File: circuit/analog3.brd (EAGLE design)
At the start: 56.2 x 50.8 mm, 76 parts, among them IC1 OP07C, IC2 74HC4052D, IC3 AD8603UJ, IC4 AD8221R, IC5 AD8221R, IC6 LM258, IC7 LM258

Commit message: - начали делать цифровую часть
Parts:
- added C27: 100n, rcl:C0603
- moved X4 0.63 mm to (22.9, 4.45), turned to 0 degrees
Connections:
- net +2.5V0: now also C27.1
- net GNDA: now also C27.2
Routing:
- net RA: track 4.55 -> 8.62 mm
- net GNDA: track 366.9 -> 369.2 mm
- net +2.5V0: track 55.0 -> 57.2 mm
- net RB: track 5.07 -> 3.54 mm
- added copper zone on layer 16, net GNDA

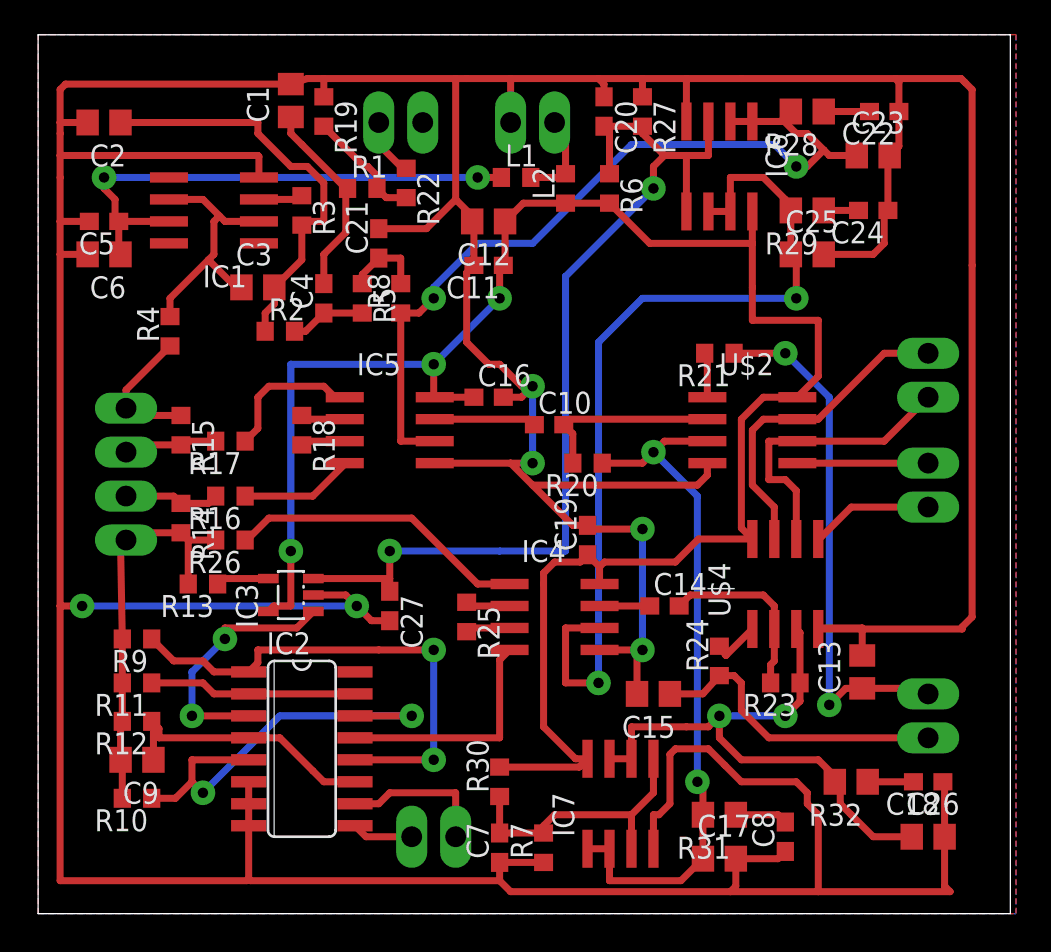
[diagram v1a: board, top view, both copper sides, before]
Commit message: - переделали аналоговую часть под более быстрый усилитель -  убрали неработающие микроиндуктивности, поставили индуктивность побольше - подставили дополнительный конденсатор на +2.5V
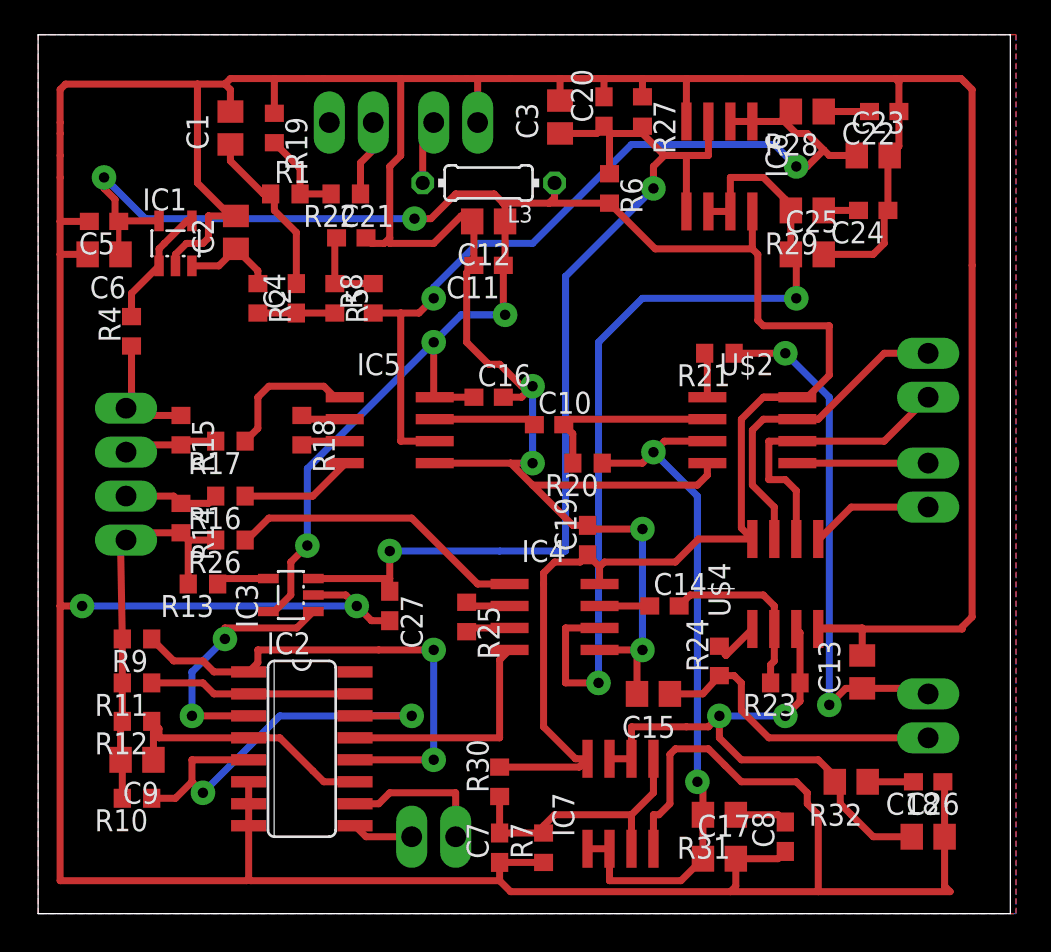
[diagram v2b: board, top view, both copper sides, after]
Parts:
- removed L1, L2: MMZ1608B102C, rcl:R0603
- removed R3: 22k, rcl:R0603
- added L3: (no value), rcl:0204/7
- C2: value 47p -> 100p
- C3: value 100p -> 10mk
- IC1: value OP07C -> AD8603UJ; device analog-devices:SO8 -> analog-devices:SOT23-5
- R18, R25: value 27k -> 18k
- moved C3 20.0 mm to (30.2, 46.0), turned to 90 degrees
- moved C2 9.92 mm to (11.4, 39.4), turned to 90 degrees
- moved R1 4.46 mm to (14.3, 41.6)
- moved X2 4.45 mm to (24.1, 45.7), turned to 180 degrees
- moved C1 3.84 mm to (11.1, 45.4)
- moved R22 3.55 mm to (17.8, 41.6), turned to 180 degrees
- moved R19 3.01 mm to (13.7, 45.4)
- moved IC1 2.93 mm to (7.94, 38.7), turned to 0 degrees
- moved X8 2.86 mm to (18.1, 45.7), turned to 0 degrees
- moved R2 2.29 mm to (12.7, 35.6), turned to 270 degrees
- moved R4 2.22 mm to (5.40, 33.7)
- moved C21 1.62 mm to (18.1, 39.1), turned to 0 degrees
- moved C4 1.59 mm to (14.9, 35.6)
- moved R5 1.59 mm to (17.1, 35.6)
- moved R8 1.59 mm to (19.4, 35.6)
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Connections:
- removed net N$7: C5.1, C6.1, IC1.7, L1.1
- removed net V+: C11.1, C12.1, C16.1, C19.1, IC3.5, IC4.8, IC5.8, IC6.8, IC7.8, L2.1, R30.2, R6.2, U$2.8, U$4.8
- net +2.5V0: now also C20.1, C3.1; no longer C20.2
- net +5V: now also C11.1, C12.1, C16.1, C19.1, C5.1, C6.1, IC1.5, IC3.5, IC4.8, IC5.8, IC6.8, IC7.8, L3.1, R30.2, R6.2, U$2.8, U$4.8; no longer L1.2, L2.2, X2.1
- net GNDA: now also C20.2, C3.2, IC1.2; no longer C20.1, IC1.4
- net N$3: now also IC1.3; no longer C3.2, R3.2
- net N$5: now also IC1.1, IC1.4; no longer C3.1, IC1.2, IC1.6
- net N$6: now also L3.2, X2.1; no longer IC1.3, R3.1
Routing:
- net +5V: track 5.32 -> 146.3 mm, vias 0 -> 5
- net V+: track 111.4 -> 0.00 mm, vias 3 -> 0
- net N$7: track 30.7 -> 0.00 mm, vias 2 -> 0
- net N$3: track 24.2 -> 5.49 mm
- net N$5: track 15.3 -> 7.14 mm
- net GNDA: track 369.2 -> 376.6 mm
- net +2.5V0: track 57.2 -> 59.6 mm
- net N$2: track 11.6 -> 9.87 mm
- net +2.5V1: track 48.0 -> 49.6 mm
- net N$34: track 6.90 -> 5.37 mm
- net N$6: track 2.57 -> 3.76 mm
- net N$19: track 8.00 -> 7.08 mm
- net GENERATOR: track 3.57 -> 4.43 mm

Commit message: - перед тем, как будем заводить SPI
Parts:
- removed C7: 100n, rcl:C0603
- removed R1: 12k, rcl:R0603
- C1: value 100p -> 10mk
- C10, C14, C4: value 100n -> 1mk
- C13, C15: value 100p -> 150p
- R27, R6: value 100k -> 120k
- moved C1 44.2 mm to (27.0, 4.13), turned to 270 degrees
- moved C6 7.96 mm to (7.62, 45.1), turned to 90 degrees
- moved C5 5.32 mm to (5.40, 45.1), turned to 90 degrees
- moved R30 0.45 mm to (27.0, 7.94)
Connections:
- removed net N$2: C1.1, C4.2, R1.1
- net GNDA: no longer C7.1
- net N$34: now also C4.2; no longer R1.2
- net N$41: now also C1.1; no longer C7.2
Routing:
- net N$34: track 5.37 -> 10.7 mm
- net N$2: track 9.87 -> 14.6 mm
- net +5V: track 146.3 -> 144.2 mm
- net GNDA: track 376.6 -> 375.1 mm

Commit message: - версия, которая почти успевает считать sin, cos свертку
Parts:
- C9: value 4.7p -> 0p
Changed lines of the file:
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@@
 <element name="R12" library="rcl" package="R0603" value="100k" x="5.715" y="11.1125" rot="R180"/>
 <element name="R13" library="rcl" package="R0603" value="1k" x="9.525" y="19.05" rot="R180"/>
-<element name="C9" library="rcl" package="C0805" value="4.7p" x="5.715" y="8.89" rot="R180"/>
+<element name="C9" library="rcl" package="C0805" value="0p" x="5.715" y="8.89" rot="R180"/>
 <element name="X1" library="con-phoenix-254" package="4POL254" value="" x="5.08" y="25.4" rot="MR270">
 <attribute name="OC_NEWARK" value="unknown" x="45.72" y="-13.97" size="1.778" layer="28" rot="MR270" display="off"/>

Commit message: C2 100 p -> 33 p R30 100 K -> 56 K - перенастроили соответственно уровни усиления
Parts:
- C2: value 100p -> 33p
- R30: value 100k -> 56k
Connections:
- net +1.6V1 renamed +2.2V1
- net +1.6V2 renamed +2.2V2
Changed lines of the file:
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@@
 <elements>
 <element name="R2" library="rcl" package="R0603" value="12k" x="12.7" y="35.56" rot="R270"/>
-<element name="C2" library="rcl" package="C0805" value="100p" x="11.43" y="39.37" rot="R90"/>
+<element name="C2" library="rcl" package="C0805" value="33p" x="11.43" y="39.37" rot="R90"/>
 <element name="C4" library="rcl" package="C0603" value="1mk" x="14.9225" y="35.56" rot="R90"/>
 <element name="C5" library="rcl" package="C0603" value="100n" x="5.3975" y="45.085" rot="R90"/>
@@
 <element name="IC7" library="linear" package="SO08" value="LM258" x="33.655" y="6.35"/>
 <element name="R7" library="rcl" package="R0603" value="47k" x="29.21" y="3.81" rot="R90"/>
-<element name="R30" library="rcl" package="R0603" value="100k" x="26.9875" y="7.9375" rot="R90"/>
+<element name="R30" library="rcl" package="R0603" value="56k" x="26.9875" y="7.9375" rot="R90"/>
 <element name="R31" library="rcl" package="R0805" value="5" x="39.37" y="5.715" rot="R180"/>
 <element name="C8" library="rcl" package="C0603" value="1mk" x="43.18" y="4.445" rot="R90"/>
@@
 <wire x1="50.585" y1="7.62" x2="47.94" y2="7.62" width="0.4064" layer="1"/>
 </signal>
-<signal name="+1.6V1">
+<signal name="+2.2V1">
 <contactref element="IC7" pad="1"/>
 <contactref element="R31" pad="2"/>
@@
 <wire x1="38.42" y1="3.175" x2="38.42" y2="5.715" width="0.4064" layer="1"/>
 </signal>
-<signal name="+1.6V2">
+<signal name="+2.2V2">
 <contactref element="IC7" pad="6"/>
 <contactref element="IC7" pad="7"/>

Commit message: - перед коррекцией по трем параметрам
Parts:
- C18, C8: value 1mk -> 4.7mk
- R31, R32: value 5 -> 22
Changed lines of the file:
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@@
 <element name="R7" library="rcl" package="R0603" value="47k" x="29.21" y="3.81" rot="R90"/>
 <element name="R30" library="rcl" package="R0603" value="56k" x="26.9875" y="7.9375" rot="R90"/>
-<element name="R31" library="rcl" package="R0805" value="5" x="39.37" y="5.715" rot="R180"/>
-<element name="C8" library="rcl" package="C0603" value="1mk" x="43.18" y="4.445" rot="R90"/>
+<element name="R31" library="rcl" package="R0805" value="22" x="39.37" y="5.715" rot="R180"/>
+<element name="C8" library="rcl" package="C0603" value="4.7mk" x="43.18" y="4.445" rot="R90"/>
 <element name="C17" library="rcl" package="C0805" value="47n" x="39.37" y="3.175"/>
-<element name="R32" library="rcl" package="R0805" value="5" x="46.99" y="7.62" rot="R180"/>
-<element name="C18" library="rcl" package="C0603" value="1mk" x="51.435" y="7.62" rot="R180"/>
+<element name="R32" library="rcl" package="R0805" value="22" x="46.99" y="7.62" rot="R180"/>
+<element name="C18" library="rcl" package="C0603" value="4.7mk" x="51.435" y="7.62" rot="R180"/>
 <element name="C26" library="rcl" package="C0805" value="47n" x="51.435" y="4.445"/>
 <element name="C27" library="rcl" package="C0603" value="100n" x="20.32" y="17.78" rot="R270"/>

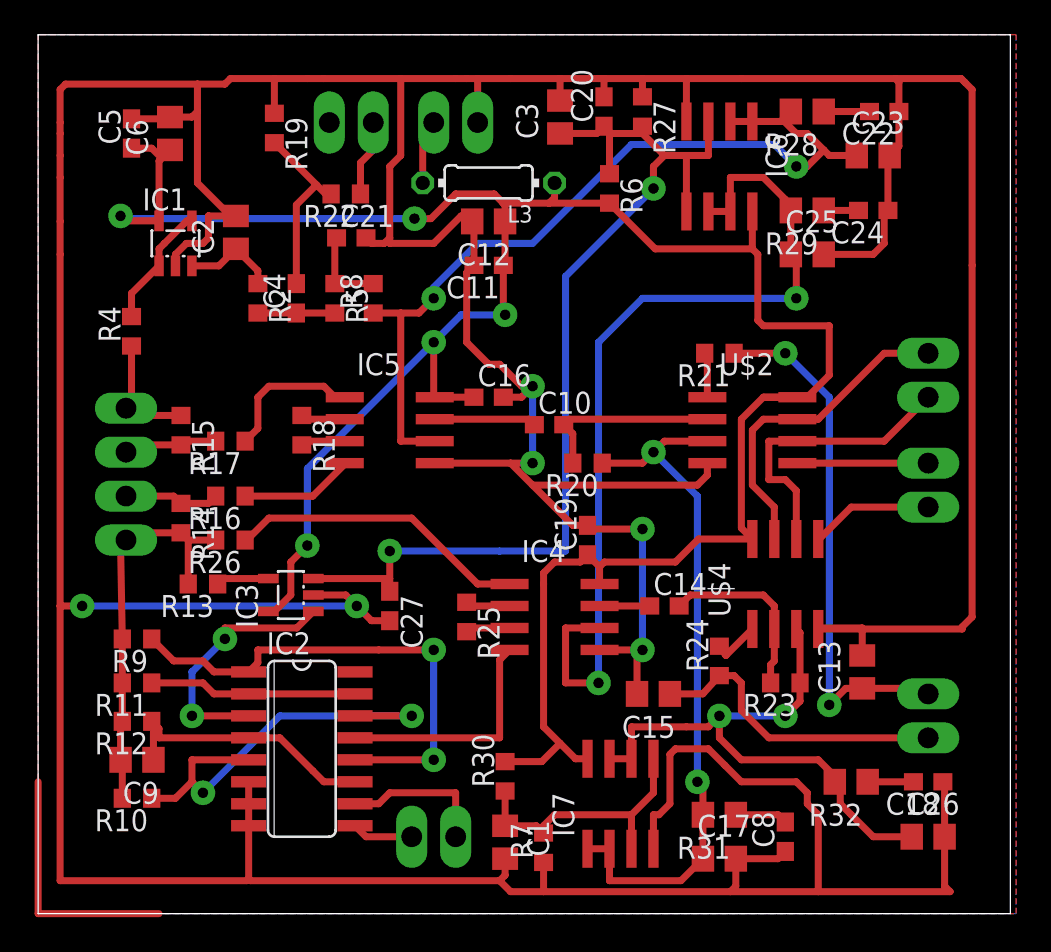
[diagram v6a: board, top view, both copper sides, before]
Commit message: - на цифровой схеме добавили разъем для Nokia 5110, коннекторы для переключения питания, объединили восточный разъем - на аналоговой схеме добавили включение 3.3 nF конденсатор, для фильтрации высокочастотных шумов ADC
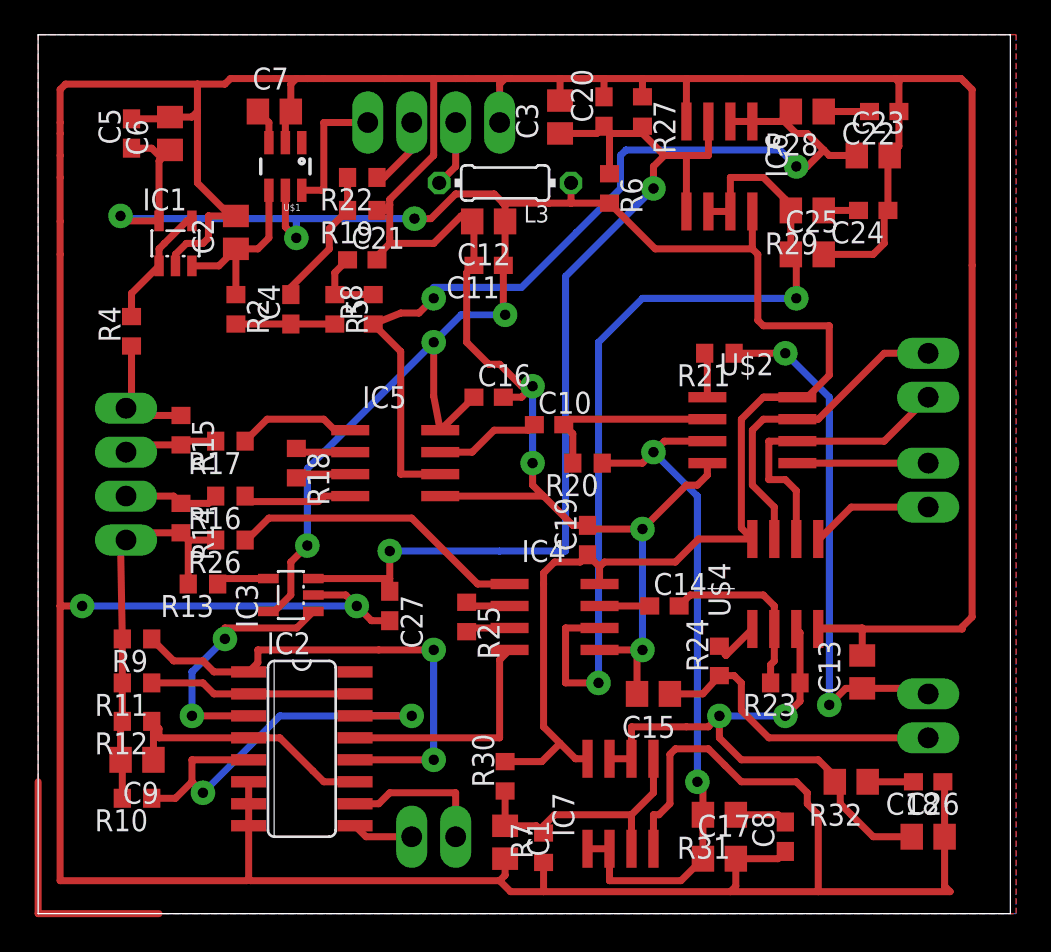
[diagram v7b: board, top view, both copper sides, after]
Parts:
- added C7: 3.3n, rcl:C0805
- added U$1: SN74LVC1G3157DBVR, balmer:SOT23-6
- C2: value 33p -> 68p
- moved R19 6.96 mm to (18.7, 40.6), turned to 180 degrees
- moved X8 2.22 mm to (20.3, 45.7)
- moved R18 1.93 mm to (14.9, 26.0)
- moved IC5 1.93 mm to (20.6, 26.0)
- moved C21 1.42 mm to (18.7, 37.8)
- moved R2 1.42 mm to (11.4, 34.9)
- moved R22 1.35 mm to (18.7, 42.5)
- moved X2 1.27 mm to (25.4, 45.7)
- moved L3 0.95 mm to (27.0, 42.2)
- moved C4 0.71 mm to (14.6, 34.9)
- moved R5 0.64 mm to (17.1, 34.9)
- moved R8 0.64 mm to (19.4, 34.9)
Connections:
- new net ANALOG_SW: U$1.6, X8.2
- new net N$7: C7.1, U$1.3
- net +5V: now also U$1.5
- net GNDA: now also C7.2, U$1.2
- net N$3: now also U$1.4
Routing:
- net ANALOG_SW: track 0.00 -> 7.67 mm
- net +5V: track 144.2 -> 150.5 mm, vias 5 -> 6
- net N$3: track 5.49 -> 10.5 mm
- net +2.5V1: track 49.6 -> 52.8 mm
- net N$34: track 10.7 -> 8.13 mm
- net GNDA: track 375.1 -> 373.0 mm
- net N$7: track 0.00 -> 2.06 mm
- net N$1: track 8.39 -> 6.86 mm
- net N$4: track 4.45 -> 5.71 mm
- net N$24: track 2.57 -> 3.20 mm
- net N$23: track 2.57 -> 3.20 mm

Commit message: - перенесли конденсаторы фильтрующие частоту для ADC на цифровую часть схемы
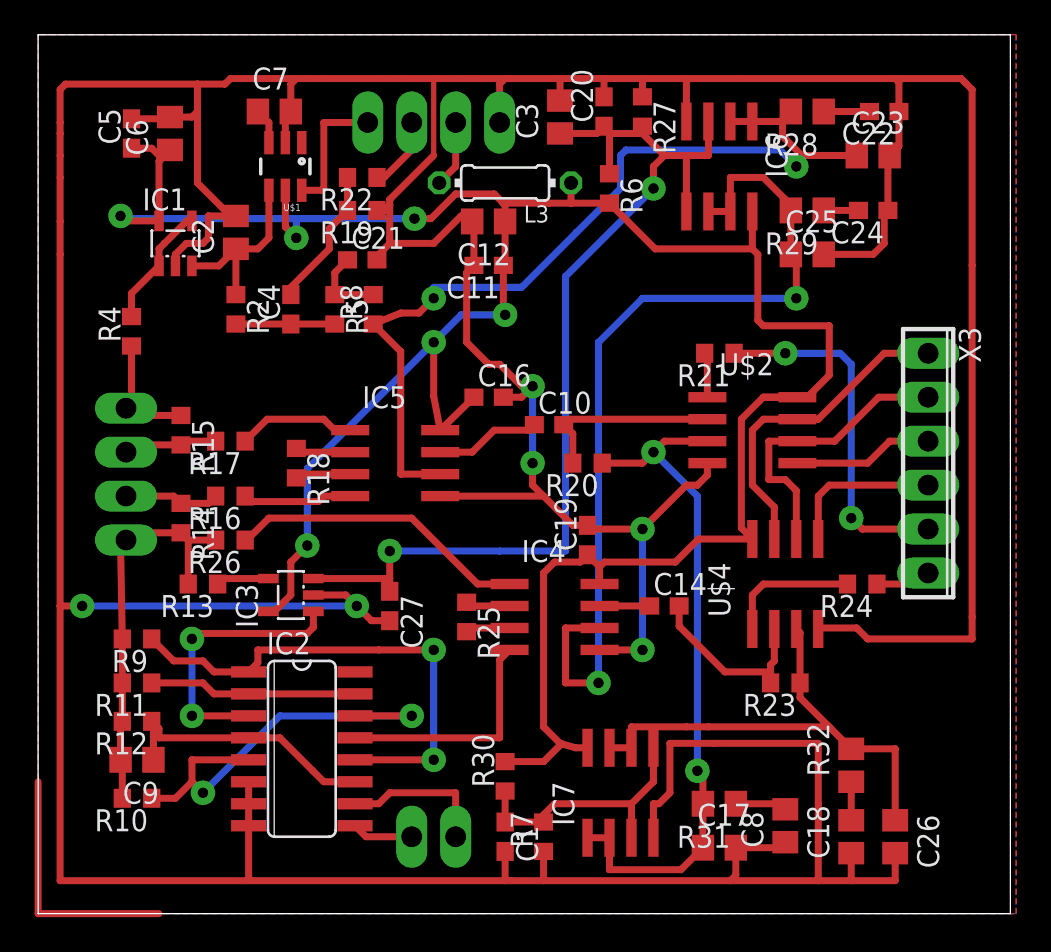
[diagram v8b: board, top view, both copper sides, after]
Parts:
- removed C13, C15: 150p, rcl:C0805
- removed X5, X6, X7: (no value), con-phoenix-254:2POL254
- added X3: (no value), con-phoenix-254:6POL254
- C1: value 10mk -> 1mk; device rcl:C0805 -> rcl:C0603
- C18, C8: value 4.7mk -> 10mk; device rcl:C0603 -> rcl:C0805
- moved R24 9.38 mm to (47.6, 19.1), turned to 180 degrees
- moved C18 5.46 mm to (47.0, 4.45), turned to 90 degrees
- moved C26 1.91 mm to (49.5, 4.45), turned to 270 degrees
- moved R32 0.95 mm to (47.0, 8.57), turned to 90 degrees
- moved IC7 0.64 mm to (33.7, 6.99)
- moved C17 0.64 mm to (39.4, 3.81)
- moved R7 0.64 mm to (29.2, 4.45)
- moved C8 0.63 mm to (43.2, 5.08)
- moved R31 0.63 mm to (39.4, 6.35)
- moved C1 0.32 mm to (27.0, 4.45)
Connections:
- net GNDA: no longer C13.2, C15.2
- net I_ADC: now also X3.6; no longer C15.1, X5.2
- net SPI_CS_I: now also X3.4; no longer X7.2
- net SPI_CS_V: now also X3.3; no longer X7.1
- net SPI_SCK: now also X3.1; no longer X6.1
- net SPI_SI: now also X3.2; no longer X6.2
- net V_ADC: now also X3.5; no longer C13.1, X5.1
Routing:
- net I_ADC: track 17.8 -> 3.22 mm
- net GNDA: track 373.0 -> 362.1 mm
- net V_ADC: track 30.6 -> 21.1 mm
- net N$26: track 2.82 -> 7.73 mm
- net +2.2V2: track 33.2 -> 28.8 mm, vias 2 -> 0
- net SPI_CS_I: track 7.11 -> 9.09 mm
- net N$11: track 14.7 -> 15.9 mm
- net +2.5V1: track 52.8 -> 52.2 mm
- net +2.2V1: track 40.3 -> 39.7 mm
- net SPI_CS_V: track 7.56 -> 8.09 mm
